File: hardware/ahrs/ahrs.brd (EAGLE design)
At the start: 160 x 100 mm, 27 parts, among them U1 LSM9DS1, U2 STM32G4_UFQFPN48_T1, X1 NX2016SA24MHZ-EXS00A-CS11335

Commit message: Laying out ahrs
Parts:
- removed C8: 100nF 10v, rcl:C0603
- added C22, C23: 0.1uF 10v, rcl:C0603
- added D1: SMAJ5A, timlib:DO-214AC
- added J1: 2-PIN, timlib:M80-8420242
- added U$5: 3-PIN, timlib:M80-8430342
- added X2: SM08B-SRSS-TB, con-jst2:SM08B-SRSS-TB
- moved C12 62.7 mm to (8.50, 21.0), turned to 180 degrees
- moved C11 55.0 mm to (9.50, 29.5), turned to 90 degrees
- moved L1 54.6 mm to (17.2, 29.5), turned to 270 degrees
- moved C3 47.1 mm to (5.00, 42.0), turned to 180 degrees
- moved U1 45.4 mm to (3.00, 28.5), turned to 270 degrees
- moved C6 45.0 mm to (11.5, 29.5), turned to 90 degrees
- moved C9 44.0 mm to (19.0, 18.0), turned to 270 degrees
- moved C13 43.0 mm to (15.5, 29.5), turned to 90 degrees
- moved C5 40.3 mm to (5.50, 31.5), turned to 180 degrees
- moved C10 39.9 mm to (17.0, 18.0), turned to 270 degrees
- moved C7 39.6 mm to (13.5, 29.5), turned to 90 degrees
- moved C21 37.2 mm to (14.5, 16.5)
- moved C2 37.0 mm to (22.0, 37.5)
- moved C14 36.5 mm to (10.0, 44.5), turned to 90 degrees
- moved C1 36.0 mm to (24.0, 46.5), turned to 90 degrees
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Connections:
- removed net LPUART1_TX: U2.10
- removed net VDD: C10.1, C11.1, C12.1, C15.1, C18.1, C2.1, C20.1, C21.1, C3.1, C5.1, C8.1, C9.1, L1.1, U$1.PIN1, U1.P$22, U1.P$23, U2.1, U2.23, U2.35, U2.48
- new net 3.3V: C10.1, C11.1, C12.1, C15.1, C18.1, C2.1, C20.1, C21.1, C22.1, C3.1, C5.1, C9.1, L1.1, U$1.PIN1, U$3.5, U1.P$22, U1.P$23, U2.1, U2.23, U2.35, U2.48, X2.1
- new net CAN_H: U$3.7, U$5.2
- new net CAN_L: U$3.6, U$5.1
- new net LPUART_RX: U2.22, X2.8
- new net LPUART_TX: U2.10, X2.3
- new net SWCLK: U2.37, X2.5
- new net SWDIO: U2.36, X2.4
- new net SWO: U2.41, X2.6
- net 5V: now also C23.1, D1.C, J1.1, U$3.3
- net CS_AG: now also U2.11
- net CS_M: now also U2.12
- net GND: now also C22.2, C23.2, D1.A, J1.2, U$3.2, U$3.PAD, U$5.3, U2.46, X2.2; no longer C8.2
- net NRST: now also X2.7
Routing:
- net 3.3V: track 0.00 -> 8.40 mm, vias 0 -> 3
- net CAN_L: track 0.00 -> 5.91 mm, vias 0 -> 1
- net 5V: track 0.00 -> 5.74 mm, vias 0 -> 1
- net CAN_H: track 0.00 -> 3.94 mm
- net GND: track 0.00 -> 2.92 mm
- added copper zone on layer 2, net 3.3V
- added copper zone on layer 2, net 5V
- added copper zone on layer 15, net GND

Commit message: R1 of ahrs
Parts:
- moved C4 20.9 mm to (7.20, 31.8)
- moved C1 18.7 mm to (13.5, 31.0)
- moved C14 17.0 mm to (5.00, 28.2)
- moved C15 16.8 mm to (2.50, 32.7), turned to 0 degrees
- moved X2 16.1 mm to (18.1, 16.6), turned to 90 degrees
- moved C10 15.5 mm to (1.60, 20.1)
- moved C11 15.3 mm to (3.90, 15.3), turned to 270 degrees
- moved L1 14.7 mm to (2.56, 30.9), turned to 0 degrees
- moved C2 14.0 mm to (9.70, 30.8), turned to 270 degrees
- moved C13 13.0 mm to (2.50, 29.2), turned to 180 degrees
- moved C3 12.8 mm to (11.5, 31.0), turned to 270 degrees
- moved C7 11.2 mm to (2.50, 27.2), turned to 180 degrees
- moved C23 11.2 mm to (6.40, 14.2)
- moved U1 9.98 mm to (10.3, 35.3), turned to 180 degrees
- moved C6 9.97 mm to (2.50, 25.2), turned to 180 degrees
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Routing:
- net GND: track 2.92 -> 52.8 mm, vias 0 -> 27
- net 3.3V: track 8.40 -> 52.5 mm, vias 3 -> 9
- net LPUART_TX: track 0.00 -> 25.4 mm, vias 0 -> 2
- net CS_M: track 0.00 -> 22.4 mm, vias 0 -> 2
- net LPUART_RX: track 0.00 -> 21.0 mm, vias 0 -> 2
- net CS_AG: track 0.00 -> 18.4 mm
- net INT_M: track 0.00 -> 18.0 mm, vias 0 -> 2
- net SCK: track 0.00 -> 17.7 mm, vias 0 -> 2
- net INT2_AG: track 0.00 -> 15.7 mm
- net MISO: track 0.00 -> 14.6 mm, vias 0 -> 2
- net INT1_AG: track 0.00 -> 14.2 mm, vias 0 -> 2
- net NRST: track 0.00 -> 13.5 mm, vias 0 -> 2
- net MOSI: track 0.00 -> 13.2 mm, vias 0 -> 2
- net SWDIO: track 0.00 -> 12.8 mm, vias 0 -> 2
- net CAN_RX: track 0.00 -> 10.8 mm, vias 0 -> 2
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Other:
- board size 160 x 100 mm -> 21 x 40 mm

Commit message: Prior to pulling from fusion
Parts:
- C1, C2, C3, C4, C5: device timlib:C0603 -> rcl:C0603
- X2: device con-jst2:SM08B-SRSS-TB -> timlib:SM08B-SRSS-TB
- moved C2 0.22 mm to (9.80, 31.0)
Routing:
- net GND: vias 27 -> 28

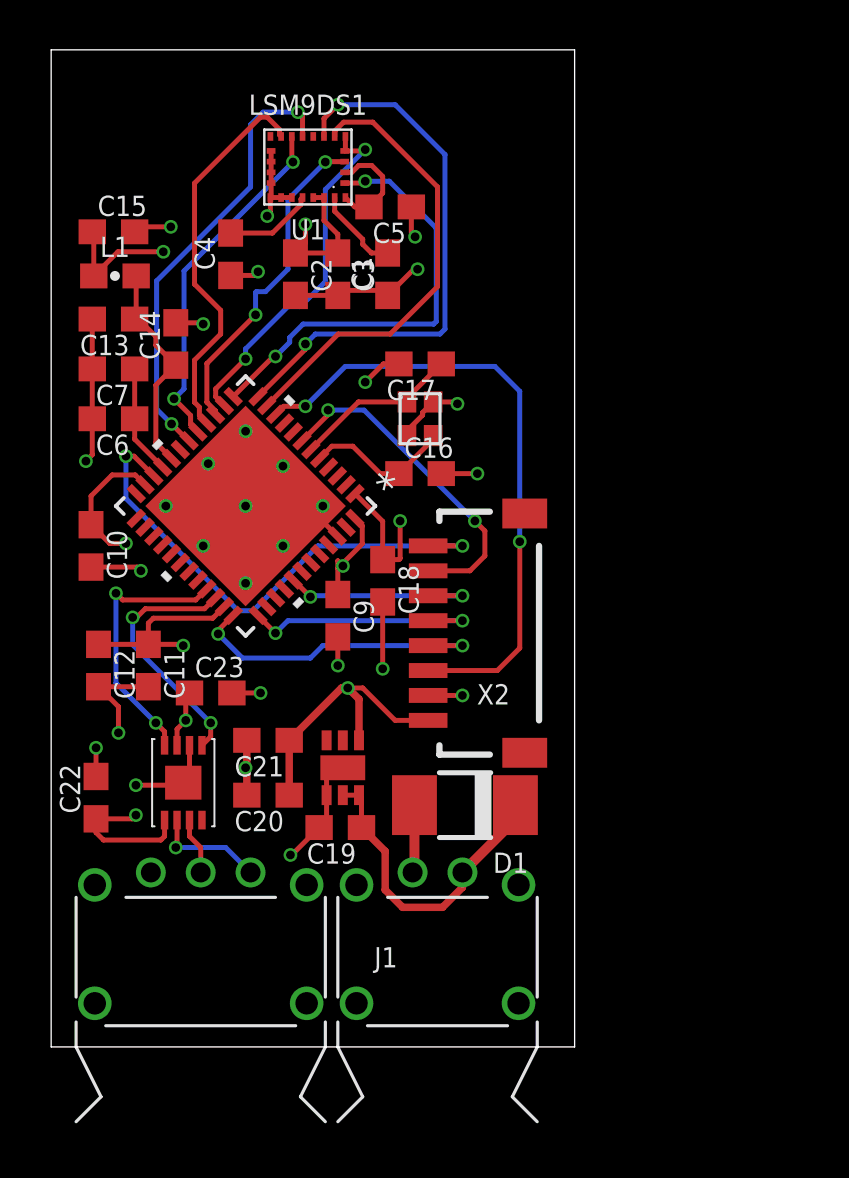
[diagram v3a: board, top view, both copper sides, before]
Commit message: Reworked AHRS to smaller footprint
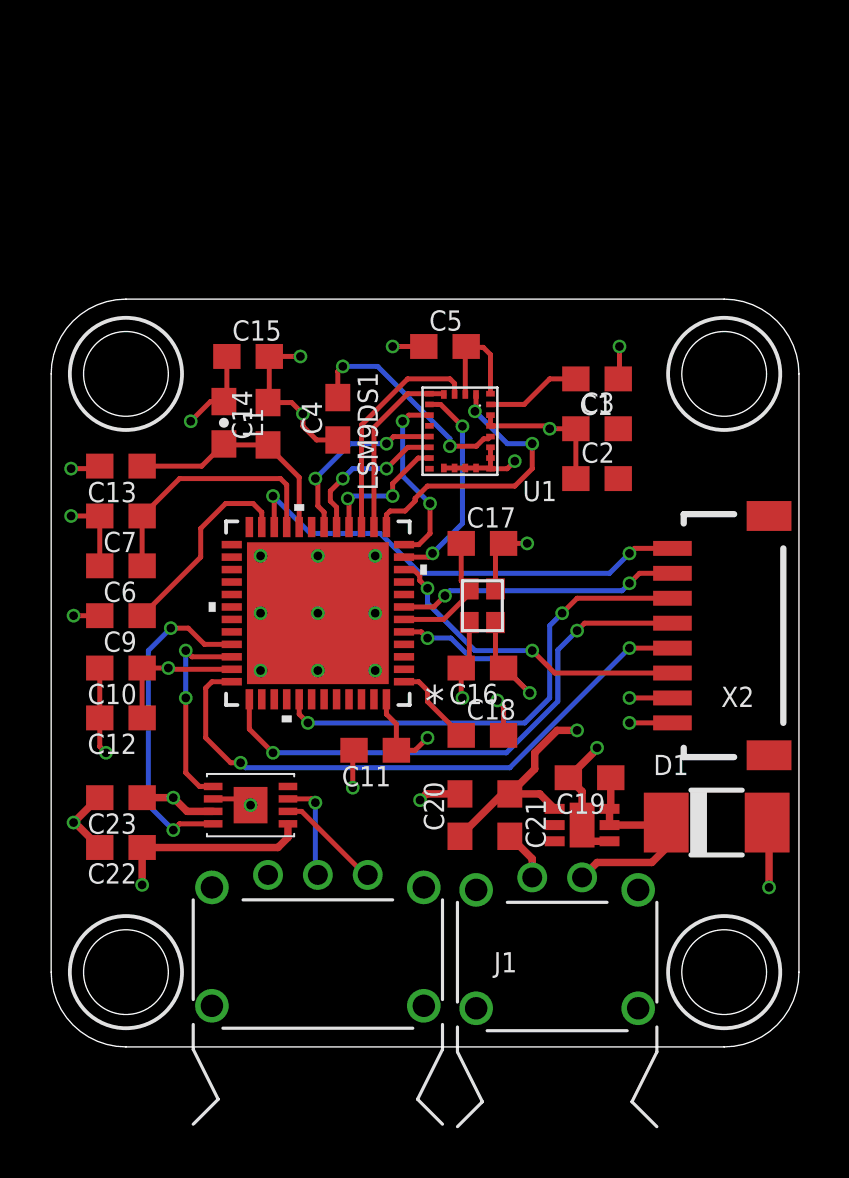
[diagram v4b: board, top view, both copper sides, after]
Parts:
- moved C2 14.6 mm to (21.9, 22.8), turned to 0 degrees
- moved U1 12.2 mm to (16.4, 24.7), turned to 270 degrees
- moved C3 12.1 mm to (21.9, 24.8), turned to 0 degrees
- moved C19 10.2 mm to (21.6, 10.8)
- moved C21 10.2 mm to (18.4, 9.30), turned to 270 degrees
- moved D1 10.1 mm to (26.7, 9.00), turned to 0 degrees
- moved U$1 9.87 mm to (21.3, 8.90), turned to 90 degrees
- moved X2 9.80 mm to (27.9, 16.5)
- moved C11 9.71 mm to (13.0, 11.9), turned to 180 degrees
- moved C1 9.39 mm to (21.9, 26.8), turned to 180 degrees
- moved C9 8.70 mm to (2.80, 17.3), turned to 180 degrees
- moved C16 8.19 mm to (17.3, 15.2), turned to 180 degrees
- moved X1 7.91 mm to (17.3, 17.7)
- moved C4 7.88 mm to (11.5, 25.2)
- moved C20 7.74 mm to (16.4, 9.30), turned to 90 degrees
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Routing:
- net CS_M: track 22.4 -> 7.36 mm
- net LPUART_TX: track 25.4 -> 12.9 mm
- net SWCLK: track 10.1 -> 21.9 mm
- net SWDIO: track 12.8 -> 24.4 mm
- net SWO: track 8.46 -> 19.5 mm
- net INT_M: track 18.0 -> 7.36 mm
- net INT2_AG: track 15.7 -> 5.41 mm, vias 0 -> 2
- net CS_AG: track 18.4 -> 8.49 mm, vias 0 -> 2
- net INT1_AG: track 14.2 -> 6.25 mm
- net MISO: track 14.6 -> 7.37 mm, vias 2 -> 0
- net SCK: track 17.7 -> 11.7 mm
- net N$1: track 4.41 -> 10.2 mm
- net N$3: track 3.60 -> 8.92 mm, vias 0 -> 2
- net GND: track 52.8 -> 48.0 mm, vias 28 -> 27
- net MOSI: track 13.2 -> 9.11 mm, vias 2 -> 0
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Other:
- board size 21 x 40 mm -> 30 x 30 mm

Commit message: Rerouting much better
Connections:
- net N$1 renamed VDDA
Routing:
- net N$3: track 8.92 -> 22.4 mm, vias 2 -> 0
- net NRST: track 11.3 -> 19.7 mm
- net LPUART_TX: track 12.9 -> 19.2 mm
- net SCK: track 11.7 -> 7.28 mm
- net CS_AG: track 8.49 -> 12.2 mm
- net SWO: track 19.5 -> 22.8 mm
- net 3.3V: track 50.2 -> 53.3 mm, vias 8 -> 10
- net N$6: track 9.48 -> 6.59 mm, vias 2 -> 0
- net CS_M: track 7.36 -> 9.51 mm
- net CAN_RX: track 13.3 -> 11.2 mm
- net MOSI: track 9.11 -> 7.41 mm, vias 0 -> 2
- net N$4: track 4.64 -> 3.38 mm
- net LPUART_RX: track 19.0 -> 18.0 mm
- net INT_M: track 7.36 -> 6.47 mm, vias 2 -> 0
- net GND: track 48.0 -> 48.7 mm, vias 27 -> 33
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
